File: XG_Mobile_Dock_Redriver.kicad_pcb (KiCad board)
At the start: 4 copper layers, 220 x 85.6 mm, 151 parts, among them J1 5-1775443-8, J10 SWD, J11 UART, J12 I2C1, J13 39301240, J14 SWD, J15 SWD, J17 8730, J2 20455-040E-76, J20 SWD, J21 SWD, J22 SWD, J23 SWD, J24 SWD, J25 SWD, J26 SWD, J27 SWD, J28 SWD, J29 SWD, J3 20455-040E-76, J30 SWD, J31 SWD, J32 SWD, J33 SWD, J4 3-2362375-4, J5 USB_C_Receptacle, J6 455860005, Q16 AO3401A, Q17 2N7002W, SW1 SW_Push, U1 DS320PR810NJXR, U12 STM32F030C8Tx, U2 DS320PR810NJXR

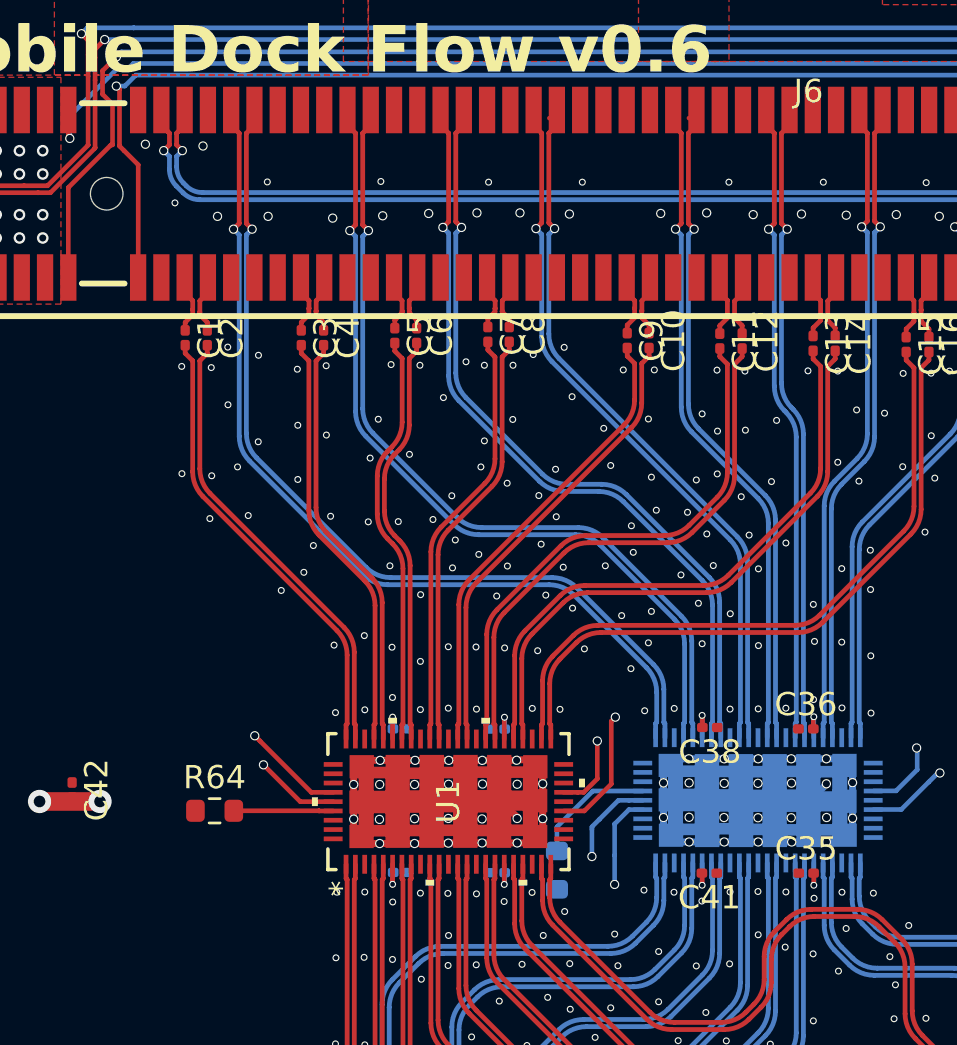
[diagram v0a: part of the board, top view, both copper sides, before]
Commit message: added more proper vias
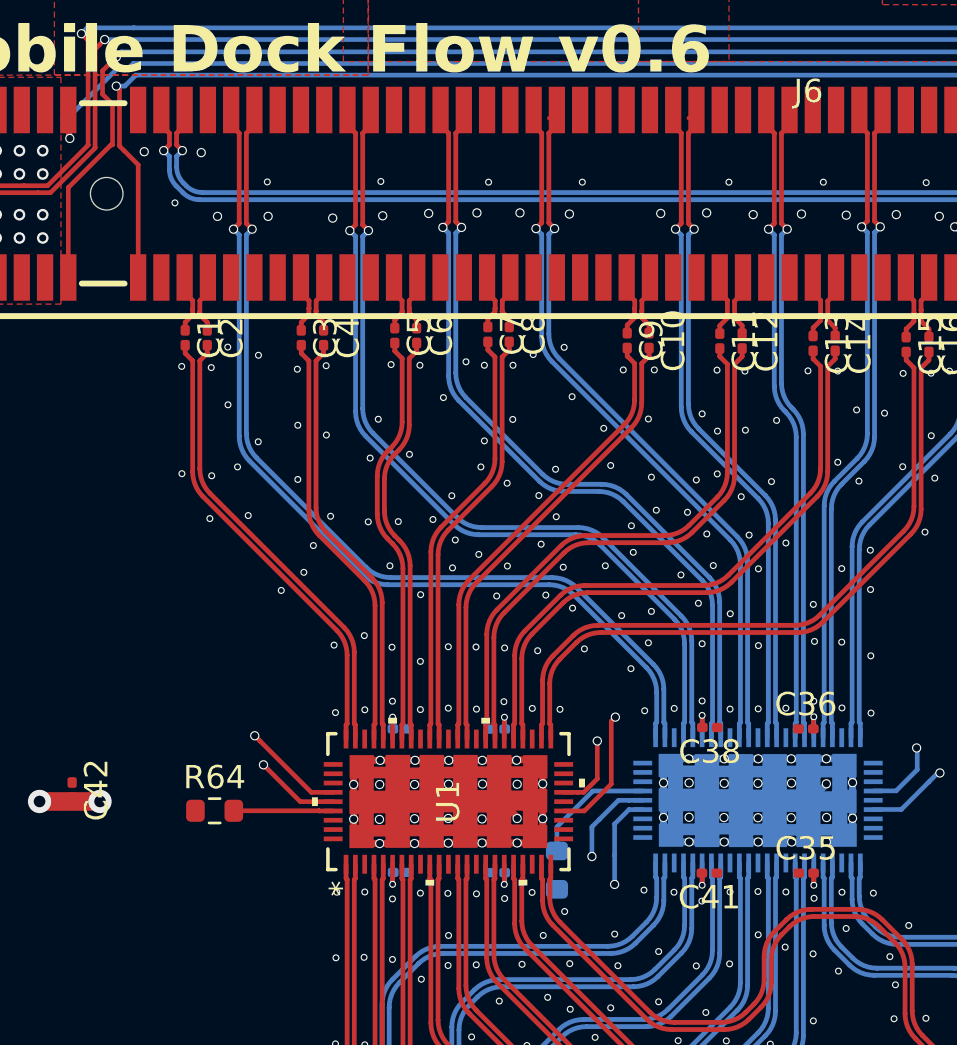
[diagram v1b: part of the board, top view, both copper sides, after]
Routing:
- net GND: vias 397 -> 399
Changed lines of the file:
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@@
+	)
+	(via
+		(at 106.66 81.96)
+		(size 0.3)
+		(drill 0.2)
+		(layers "F.Cu" "B.Cu")
+		(free yes)
+		(net 1)
 	)
 	(via
@@
 	)
 	(via
-		(at 93.725 58.075)
+		(at 93.65 58.36)
 		(size 0.4)
 		(drill 0.3)
@@
 	)
 	(via
-		(at 101.87 81.78)
+		(at 101.87 81.94)
 		(size 0.3)
 		(drill 0.2)
@@
 	)
 	(via
-		(at 101.88 90.57)
+		(at 101.87 90.44)
 		(size 0.3)
 		(drill 0.2)
@@
 	)
 	(via
-		(at 91.25 58)
+		(at 91.2 58.32)
 		(size 0.4)
 		(drill 0.3)
@@
 	)
 	(via
+		(at 115.18 81.93)
+		(size 0.3)
+		(drill 0.2)
+		(layers "F.Cu" "B.Cu")
+		(free yes)
+		(net 1)
+	)
+	(via
 		(at 100.65 92.95)
 		(size 0.3)
@@
 	)
 	(via
-		(at 106.67 90.55)
+		(at 106.69 90.42)
 		(size 0.3)
 		(drill 0.2)
@@
 	)
 	(via
-		(at 119.97 81.87)
-		(size 0.3)
-		(drill 0.2)
+		(at 119.98 81.94)
+		(size 0.3)
+		(drill 0.2)

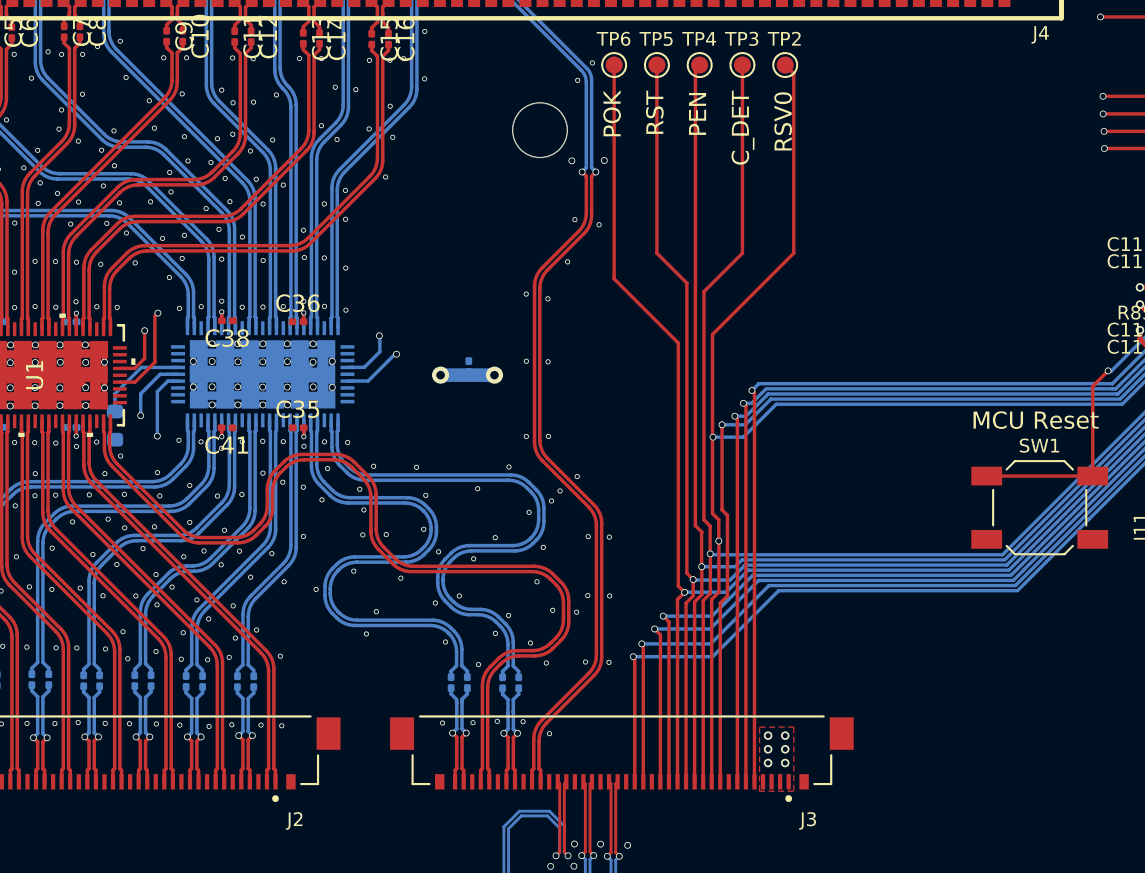
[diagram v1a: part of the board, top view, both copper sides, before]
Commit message: tweaked traces
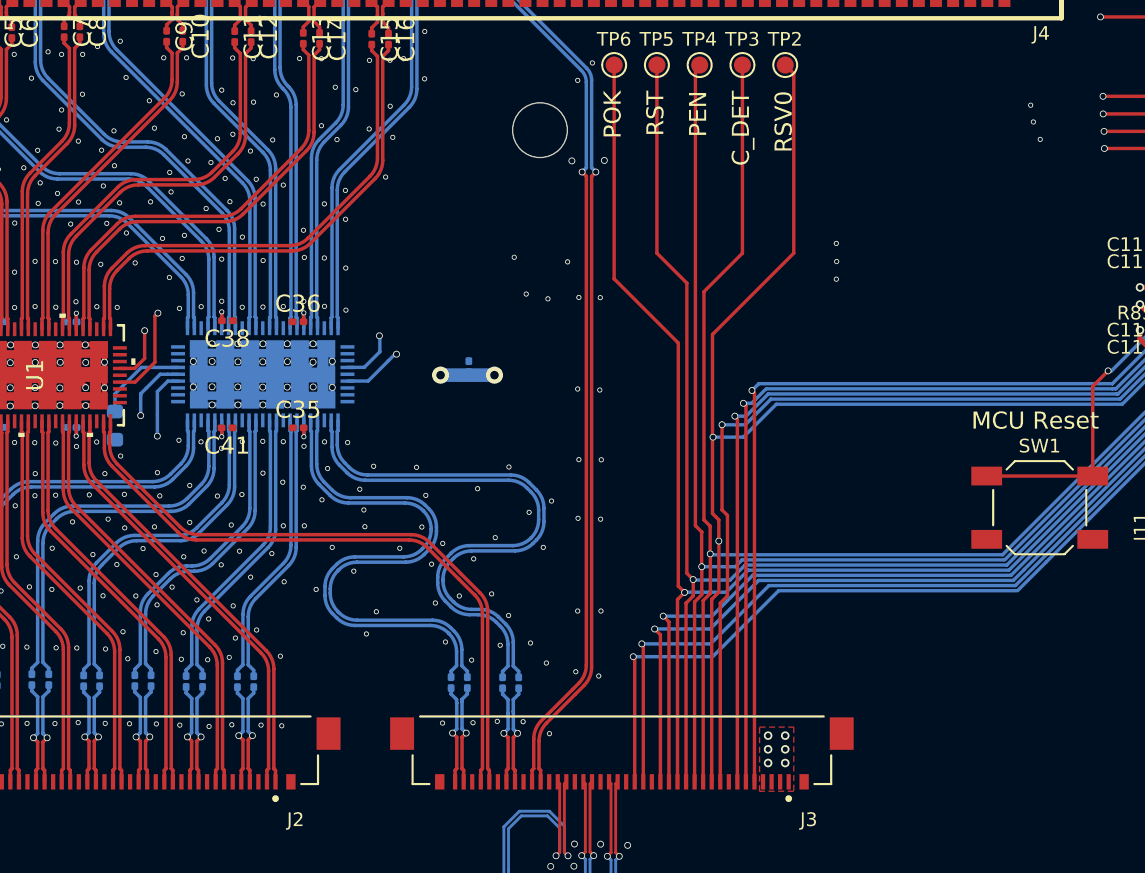
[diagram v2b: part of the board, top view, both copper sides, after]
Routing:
- net /HSOL7P: track 52.7 -> 38.0 mm
- net /HSOL7N: track 52.7 -> 38.0 mm
- net /CLKP: track 96.5 -> 93.8 mm
- net /CLKN: track 96.6 -> 93.9 mm
- net GND: vias 399 -> 404

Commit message: more tweaks
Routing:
- net GND: vias 404 -> 413
- net /RSV0: vias 3 -> 2
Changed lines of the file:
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@@
 	)
 	(via
+		(at 97.4 73.95)
+		(size 0.3)
+		(drill 0.2)
+		(layers "F.Cu" "B.Cu")
+		(free yes)
+		(net 1)
+	)
+	(via
 		(at 121.645 86.97)
 		(size 0.4)
@@
 	)
 	(via
-		(at 116.22 96.54)
+		(at 116.69 96.4)
 		(size 0.3)
 		(drill 0.2)
@@
 	)
 	(via
-		(at 115.15 97.34)
+		(at 115.16 97.35)
 		(size 0.3)
 		(drill 0.2)
@@
 	)
 	(via
+		(at 117.83 67.75)
+		(size 0.3)
+		(drill 0.2)
+		(layers "F.Cu" "B.Cu")
+		(free yes)
+		(net 1)
+	)
+	(via
 		(at 102.38 102.1)
 		(size 0.3)
@@
 	)
 	(via
+		(at 106.24 74.04)
+		(size 0.3)
+		(drill 0.2)
+		(layers "F.Cu" "B.Cu")
+		(free yes)
+		(net 1)
+	)
+	(via
 		(at 117.59 82.27)
 		(size 0.3)
@@
 	)
 	(via
+		(at 119.07 67.72)
+		(size 0.3)
+		(drill 0.2)
+		(layers "F.Cu" "B.Cu")
+		(free yes)
+		(net 1)
+	)
+	(via
 		(at 134.34 107.21)
 		(size 0.3)
@@
 	)
 	(via
+		(at 104.31 94.8)
+		(size 0.3)
+		(drill 0.2)
+		(layers "F.Cu" "B.Cu")
+		(free yes)
+		(net 1)
+	)
+	(via
 		(at 116.33 59.63)
 		(size 0.3)
@@
 	)
 	(via
+		(at 101.05 67.01)
+		(size 0.3)
+		(drill 0.2)
+		(layers "F.Cu" "B.Cu")
+		(free yes)
+		(net 1)
+	)
+	(via
+		(at 99.81 67.03)
+		(size 0.3)
+		(drill 0.2)
+		(layers "F.Cu" "B.Cu")
+		(free yes)
+		(net 1)
+	)
+	(via
 		(at 104.06 68.89)
 		(size 0.3)
@@
 	)
 	(via
+		(at 117.51 94.84)
+		(size 0.3)
+		(drill 0.2)
+		(layers "F.Cu" "B.Cu")
+		(free yes)
+		(net 1)
+	)
+	(via
 		(at 119.02 85.46)
 		(size 0.4)
@@
 	)
 	(via
+		(at 93.62 59.58)
+		(size 0.3)
+		(drill 0.2)
+		(layers "F.Cu" "B.Cu")
+		(free yes)
+		(net 1)
+	)
+	(via
 		(at 119.96 77.78)
 		(size 0.3)
@@
 		(size 0.4)
 		(drill 0.3)
-		(layers "F.Cu" "B.Cu")
-		(net 144)
-	)
-	(via
-		(at 144.24 95.95)
-		(size 0.4)
-		(drill 0.3)
